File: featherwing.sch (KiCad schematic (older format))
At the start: 3 parts, among them J9 GROVE-SMD-90D, U1 ROF-78E

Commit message: Updated master layout
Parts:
- removed J9: GROVE-SMD-90D, ATM90E26_from_eagle:SEEED-CONNECTOR--2016_HW4-SMD-2.0-90D, symbol SEEED-CONNECTOR--2016_GROVE-CONNECTOR-SMD-90D_4+2P-2.0_
- added C22: 1u/16V, Capacitors_SMD:C_0603, symbol C_Small
- added C23: 100u/16V, Capacitors_SMD:CP_Elec_5x5.8, symbol CP
- added C24: 1u/50V, Capacitors_SMD:C_0603, symbol C_Small
- added C25: 220u/50V, Capacitors_SMD:CP_Elec_8x10, symbol CP
- added D5: LED, LEDs:LED_0603, symbol LED
- added D6, D7, D8, D9: D_Schottky, Diodes_SMD:D_SOD-123, symbol D_Schottky
- added J10: GROVE-SMD-90D, ATM90E26_from_eagle:SEEED-CONNECTOR--2016_HW4-SMD-2.0-90D, symbol SEEED-CONNECTOR--2016_GROVE-CONNECTOR-SMD-90D_4+2P-2.0_
- added J9: GS3, Connectors:GS3, symbol GS3
- added JP1: Jumper_NC_Small, Connectors:GS2, symbol Jumper
- added LOGO2: LOGO, symbol LOGO
- added R29: R, Resistors_SMD:R_0603_HandSoldering, symbol R
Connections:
- net +3V3: now also J10.3
- net GND: now also U1.2 (GND), C22.2, C23.2, C24.2, C25.2, D5.1 (K), J10.4, J10.SS1, J10.SS2
- net at U1.1 (VIN): now also C24.1, C25.1, D7.1 (K), D8.1 (K), D9.1 (K)
- net at U1.3 (VOUT): now also C22.1, C23.1, D6.2 (A), JP1.2; no longer MS1.26 (USB)
- net SCK: now reaches MS1.11 (GPIOSCK)
- net MOSI: now reaches MS1.12 (GPIOMOSI)
- net MISO: now reaches MS1.13 (GPIOMISO)
- net at MS1.17 (GPIOSDA): now also J10.2
- net at MS1.18 (GPIOSCL): now also J10.1
- net at MS1.21 (GPIO9): now also J9.3 (G3)
- net at MS1.22 (GPIO10): now also J9.1 (G1)
- new net: D5.2 (A), R29.2
- new net: JP1.1, R29.1
- new net CS: J9.2 (G2)
- new net UA: D7.2 (A)
- new net UB: D8.2 (A)
- new net UC: D9.2 (A)
- new net USB: D6.1 (K), MS1.26 (USB)
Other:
- note added: "Feather Connector"
- note added: "Rectifier and Regulator"

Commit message: Playing with autoplace
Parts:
- D7, D8, D9: footprint Diodes_SMD:D_SOD-123 -> Diodes_SMD:D_SMA
- LOGO2: footprint (none) -> Whatnick_logo:Whatnick_logo
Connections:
- net +3V3: now also MS1.2 (3V)
- net GND: now also MS1.4 (GND)
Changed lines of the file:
@@
 F 0 "D7" H 5950 3250 50  0000 C CNN
 F 1 "D_Schottky" H 5950 3050 50  0000 C CNN
-F 2 "Diodes_SMD:D_SOD-123" H 5950 3150 50  0001 C CNN
+F 2 "Diodes_SMD:D_SMA" H 5950 3150 50  0001 C CNN
 F 3 "" H 5950 3150 50  0001 C CNN
 	1    5950 3150
@@
 F 0 "D8" H 5950 3550 50  0000 C CNN
 F 1 "D_Schottky" H 5950 3350 50  0000 C CNN
-F 2 "Diodes_SMD:D_SOD-123" H 5950 3450 50  0001 C CNN
+F 2 "Diodes_SMD:D_SMA" H 5950 3450 50  0001 C CNN
 F 3 "" H 5950 3450 50  0001 C CNN
 	1    5950 3450
@@
 F 0 "D9" H 5950 3900 50  0000 C CNN
 F 1 "D_Schottky" H 5950 3700 50  0000 C CNN
-F 2 "Diodes_SMD:D_SOD-123" H 5950 3800 50  0001 C CNN
+F 2 "Diodes_SMD:D_SMA" H 5950 3800 50  0001 C CNN
 F 3 "" H 5950 3800 50  0001 C CNN
 	1    5950 3800
@@
 L LOGO LOGO2
 U 1 1 597B65BD
-P 5400 6200
-F 0 "LOGO2" H 5400 6098 60  0001 C CNN
-F 1 "LOGO" H 5400 6302 60  0001 C CNN
-F 2 "" H 5400 6200 60  0001 C CNN
-F 3 "" H 5400 6200 60  0001 C CNN
-	1    5400 6200
-	1    0    0    -1
-$EndComp
+P 3550 1450
+F 0 "LOGO2" H 3550 1348 60  0001 C CNN
+F 1 "LOGO" H 3550 1552 60  0001 C CNN
+F 2 "Whatnick_logo:Whatnick_logo" H 3550 1450 60  0001 C CNN
+F 3 "" H 3550 1450 60  0001 C CNN
+	1    3550 1450
+	1    0    0    -1
+$EndComp
+Wire Wire Line
+	8000 4650 8000 4800
+Wire Wire Line
+	8200 4650 8200 4800
+Text GLabel 8000 4800 3    60   Input ~ 0
++3V3
+Text GLabel 8200 4800 3    60   Input ~ 0
+GND
 $EndSCHEMATC

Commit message: Place completed
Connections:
- net VIN: now reaches C24.1, C25.1, D7.1 (K), D8.1 (K), D9.1 (K), U1.1 (VIN)
- net VOUT: now reaches C22.1, C23.1, D6.2 (A), JP1.2, U1.3 (VOUT)
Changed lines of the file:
@@
 Text GLabel 8200 4800 3    60   Input ~ 0
 GND
+Text Label 4350 3150 0    60   ~ 0
+VIN
+Text Label 2800 3150 0    60   ~ 0
+VOUT
 $EndSCHEMATC

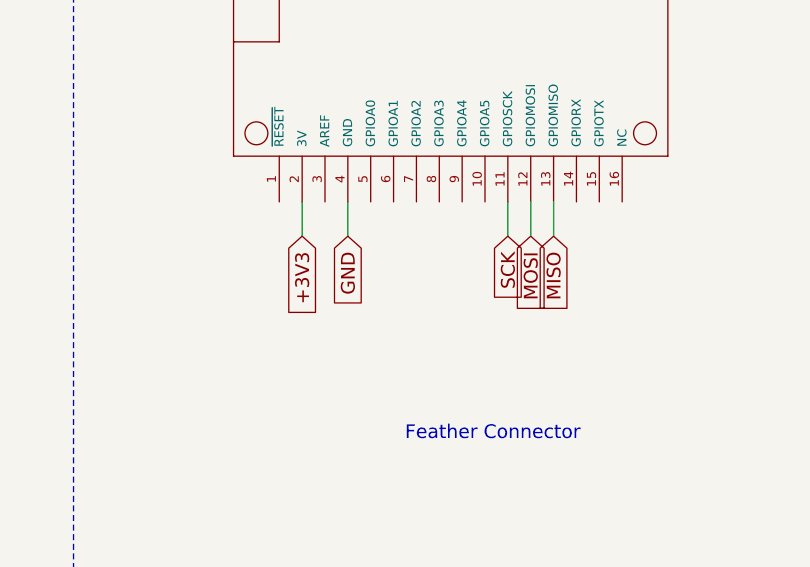
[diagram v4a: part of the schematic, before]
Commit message: Fixed global names after ERC
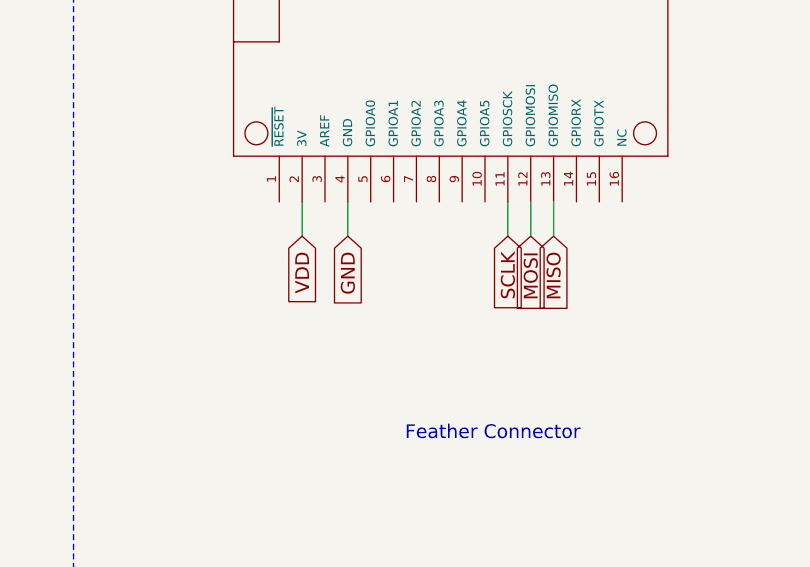
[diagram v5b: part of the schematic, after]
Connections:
- net +3V3: no longer MS1.2 (3V)
- net SCK renamed SCLK
- new net VDD: MS1.2 (3V)
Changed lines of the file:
@@
 	9000 2950 9000 2800
 Text GLabel 8900 4800 3    60   Input ~ 0
-SCK
+SCLK
 Text GLabel 9000 4800 3    60   Input ~ 0
 MOSI
@@
 	8200 4650 8200 4800
 Text GLabel 8000 4800 3    60   Input ~ 0
-+3V3
+VDD
 Text GLabel 8200 4800 3    60   Input ~ 0
 GND

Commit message: Reroute to kicad nightly
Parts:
- C22, C24: symbol C_Small -> device:C_Small
- C23, C25: symbol CP -> device:CP
- D5: symbol LED -> device:LED
- D6, D7, D8, D9: symbol D_Schottky -> device:D_Schottky
- J10: symbol SEEED-CONNECTOR--2016_GROVE-CONNECTOR-SMD-90D_4+2P-2.0_ -> ATM90E26_Featherwing:SEEED-CONNECTOR--2016_GROVE-CONNECTOR-SMD-90D_4+2P-2.0_
- J9: symbol GS3 -> ATM90E3x_fw-rescue:GS3-RESCUE-ATM90E3x_fw
- JP1: symbol Jumper -> device:Jumper
- LOGO2: symbol LOGO -> whatnick:LOGO
- MS1: symbol ADAFRUIT_FEATHERWING -> ATM90E26_Featherwing:ADAFRUIT_FEATHERWING
- R29: symbol R -> device:R
- U1: symbol ROF-78E -> ROF-78E:ROF-78E
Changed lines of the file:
@@
-EESchema Schematic File Version 2
-LIBS:power
-LIBS:device
-LIBS:transistors
-LIBS:conn
-LIBS:linear
-LIBS:regul
-LIBS:74xx
-LIBS:cmos4000
-LIBS:adc-dac
-LIBS:memory
-LIBS:xilinx
-LIBS:microcontrollers
-LIBS:dsp
-LIBS:microchip
-LIBS:analog_switches
-LIBS:motorola
-LIBS:texas
-LIBS:intel
-LIBS:audio
-LIBS:interface
-LIBS:digital-audio
-LIBS:philips
-LIBS:display
-LIBS:cypress
-LIBS:siliconi
-LIBS:opto
-LIBS:atmel
-LIBS:contrib
-LIBS:valves
-LIBS:ATM90E36_Breakout
-LIBS:ROF-78E
-LIBS:ATM90E26_Featherwing
-LIBS:whatnick
+EESchema Schematic File Version 4
 LIBS:ATM90E3x_fw-cache
 EELAYER 26 0
@@
 $EndDescr
 $Comp
-L ROF-78E U1
+L ROF-78E:ROF-78E U1
 U 1 1 597B3E83
 P 2750 3450
@@
 $EndComp
 $Comp
-L ADAFRUIT_FEATHERWING MS1
+L ATM90E26_Featherwing:ADAFRUIT_FEATHERWING MS1
 U 1 1 597B3E84
 P 7700 4450
@@
 $EndComp
 $Comp
-L SEEED-CONNECTOR--2016_GROVE-CONNECTOR-SMD-90D_4+2P-2.0_ J10
+L ATM90E26_Featherwing:SEEED-CONNECTOR--2016_GROVE-CONNECTOR-SMD-90D_4+2P-2.0_ J10
 U 1 1 597B3E85
 P 10300 2300
@@
 $EndComp
 $Comp
-L +3V3 #PWR19
+L power:+3V3 #PWR019
 U 1 1 597B3E86
 P 9750 2700
-F 0 "#PWR19" H 9750 2550 50  0001 C CNN
+F 0 "#PWR019" H 9750 2550 50  0001 C CNN
 F 1 "+3V3" V 9765 2828 50  0000 L CNN
 F 2 "" H 9750 2700 50  0001 C CNN
@@
 $EndComp
 $Comp
-L GND #PWR20
+L power:GND #PWR020
 U 1 1 597B3E87
 P 9850 2700
-F 0 "#PWR20" H 9850 2450 50  0001 C CNN
+F 0 "#PWR020" H 9850 2450 50  0001 C CNN
 F 1 "GND" H 9855 2527 50  0000 C CNN
 F 2 "" H 9850 2700 50  0001 C CNN
@@
 $EndComp
 $Comp
-L CP C25
+L device:CP C25
 U 1 1 597B3E89
 P 5050 3350
@@
 $EndComp
 $Comp
-L CP C23
+L device:CP C23
 U 1 1 597B3E8A
 P 2650 3500
@@
 $EndComp
 $Comp
-L C_Small C24
+L device:C_Small C24
 U 1 1 597B3E8B
 P 4650 3350
@@
 $EndComp
 $Comp
-L C_Small C22
+L device:C_Small C22
 U 1 1 597B3E8C
 P 2200 3550
@@
 $EndComp
 $Comp
-L D_Schottky D7
+L device:D_Schottky D7
 U 1 1 597B3E8D
 P 5950 3150
@@
 $EndComp
 $Comp
-L D_Schottky D8
+L device:D_Schottky D8
 U 1 1 597B3E8E
 P 5950 3450
@@
 $EndComp
 $Comp
-L D_Schottky D9
+L device:D_Schottky D9
 U 1 1 597B3E8F
 P 5950 3800
@@
 $EndComp
 $Comp
-L D_Schottky D6
+L device:D_Schottky D6
 U 1 1 597B3E90
 P 2400 2850
@@
 $EndComp
 $Comp
-L LED D5
+L device:LED D5
 U 1 1 597B3E91
 P 950 3950
@@
 $EndComp
 $Comp
-L R R29
+L device:R R29
 U 1 1 597B3E92
 P 950 3450
@@
 $EndComp
 $Comp
-L Jumper JP1
+L device:Jumper JP1
 U 1 1 597B3E93
 P 1650 3150
@@
 UA
 $Comp
-L GND #PWR18
+L power:GND #PWR018
 U 1 1 597B3E94
 P 3550 4400
-F 0 "#PWR18" H 3550 4150 50  0001 C CNN
+F 0 "#PWR018" H 3550 4150 50  0001 C CNN
 F 1 "GND" H 3555 4227 50  0000 C CNN
 F 2 "" H 3550 4400 50  0001 C CNN
@@
 	10100 2450 9850 2450
 Wire Wire Line
-	9850 2450 9850 2700
-Wire Wire Line
-	9850 2600 10600 2600
+	9850 2450 9850 2600
+Wire Wire Line
+	9850 2600 10300 2600
 Connection ~ 9850 2600
 Wire Wire Line
@@
 	9400 2250 10100 2250
 Wire Wire Line
-	1950 3150 3050 3150
+	1950 3150 2200 3150
 Wire Wire Line
 	1350 3150 950  3150
@@
 	950  4100 950  4250
 Wire Wire Line
-	950  4250 6200 4250
-Wire Wire Line
-	3550 3750 3550 4400
+	950  4250 2200 4250
+Wire Wire Line
+	3550 3750 3550 4250
 Wire Wire Line
 	2650 3650 2650 4250
@@
 	4650 3250 4650 3150
 Wire Wire Line
-	4050 3150 5800 3150
+	4050 3150 4650 3150
 Wire Wire Line
 	5050 3150 5050 3200
@@
 	5800 3450 5500 3450
 Wire Wire Line
-	5500 3150 5500 3800
+	5500 3150 5500 3450
 Connection ~ 5500 3150
 Wire Wire Line
@@
 MISO
 $Comp
-L GS3 J9
+L ATM90E3x_fw-rescue:GS3-RESCUE-ATM90E3x_fw J9
 U 1 1 597B52FB
 P 8950 2550
@@
 Feather Connector
 $Comp
-L LOGO LOGO2
+L whatnick:LOGO LOGO2
 U 1 1 597B65BD
 P 3550 1450
@@
 Text Label 2800 3150 0    60   ~ 0
 VOUT
+Wire Wire Line
+	9850 2600 9850 2700
+Wire Wire Line
+	10300 2600 10600 2600
+Wire Wire Line
+	2650 4250 3550 4250
+Wire Wire Line
+	2200 4250 2650 4250
+Wire Wire Line
+	2200 3150 2400 3150
+Wire Wire Line
+	2650 3150 3050 3150
+Wire Wire Line
+	3550 4250 3550 4400
+Wire Wire Line
+	3550 4250 4650 4250
+Wire Wire Line
+	4650 3150 5050 3150
+Wire Wire Line
+	4650 4250 5050 4250
+Wire Wire Line
+	2400 3150 2650 3150
+Wire Wire Line
+	5050 3150 5500 3150
+Wire Wire Line
+	5500 3150 5800 3150
+Wire Wire Line
+	5500 3450 5500 3800
+Wire Wire Line
+	5050 4250 6200 4250
 $EndSCHEMATC

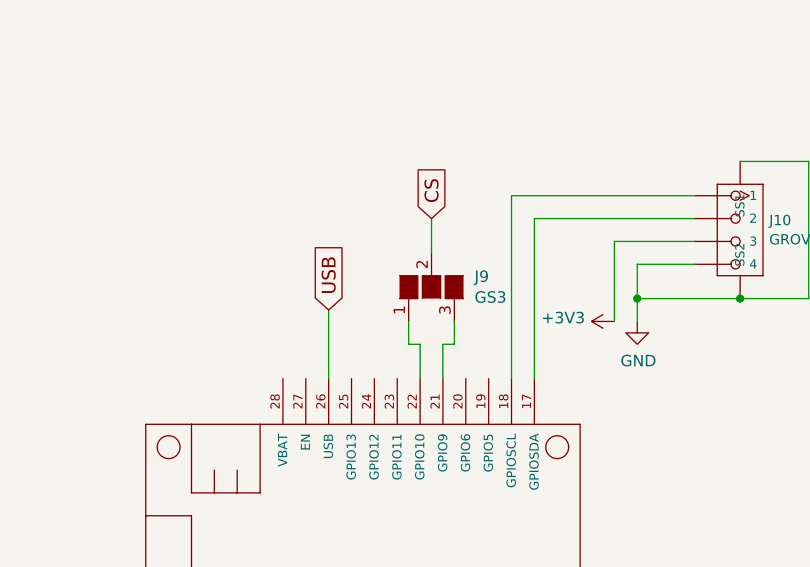
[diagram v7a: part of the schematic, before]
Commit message: Update gerbers and add default chip select
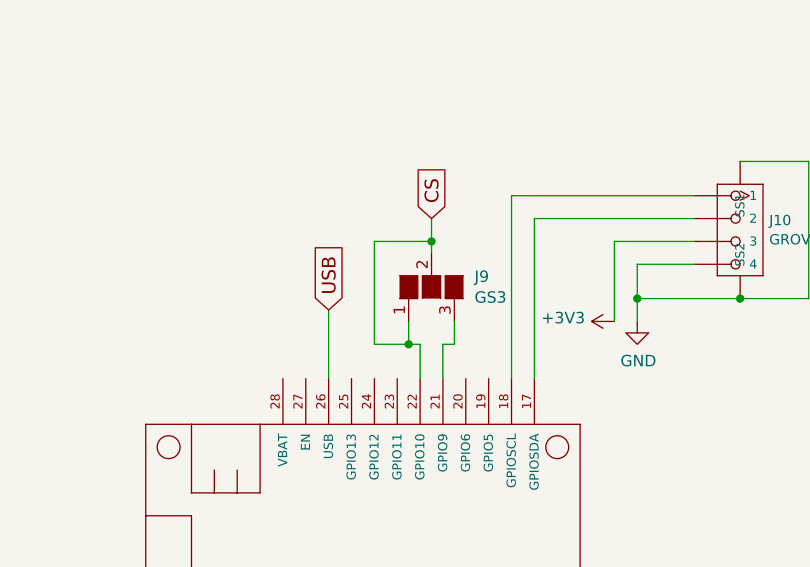
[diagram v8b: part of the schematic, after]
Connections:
- net CS: now also J9.1 (G1), MS1.22 (GPIO10)
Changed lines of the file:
@@
 	9050 2800 9050 2700
 Wire Wire Line
-	8950 2400 8950 2250
+	8950 2400 8950 2350
 Text GLabel 8950 2250 1    60   Input ~ 0
 CS
@@
 Wire Wire Line
 	5050 4250 6200 4250
+Wire Wire Line
+	8850 2800 8700 2800
+Wire Wire Line
+	8700 2800 8700 2350
+Wire Wire Line
+	8700 2350 8950 2350
+Connection ~ 8850 2800
+Connection ~ 8950 2350
+Wire Wire Line
+	8950 2350 8950 2250
 $EndSCHEMATC
